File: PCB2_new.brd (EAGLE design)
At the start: 100 x 80 mm, 106 parts

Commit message: PCB2 for remote work
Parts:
- added R1, R2, R3: 330k, rcl:M0805
- moved H2 114.1 mm to (69.6, 19.6)
- moved H1 50.9 mm to (14.0, 11.4)
- moved SJ1 1.27 mm to (6.10, 19.9), flipped to the bottom, turned to 180 degrees
- moved SJ2 0.51 mm to (92.7, 18.5), flipped to the bottom, turned to 180 degrees
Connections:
- new net N$31: PAD3.1, R3.1
- net FRET3: now also R1.1, R1.2
- net FRET4: now also R2.1, R2.2
- net FRET5: now also R3.2; no longer PAD3.1
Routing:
- net VDD: track 0.00 -> 108.6 mm, vias 0 -> 2
- net FRET5: track 25.3 -> 14.7 mm, vias 0 -> 1
- net N$31: track 0.00 -> 9.09 mm
- net G: track 92.8 -> 98.6 mm
- net FRET4: track 65.4 -> 61.7 mm
- net GND: track 244.4 -> 246.4 mm
- net FRET3: track 89.9 -> 91.6 mm
- net LED_SER5: track 98.9 -> 97.6 mm
- net LED_SER6: track 52.2 -> 51.4 mm
- net RCK: track 67.9 -> 68.6 mm

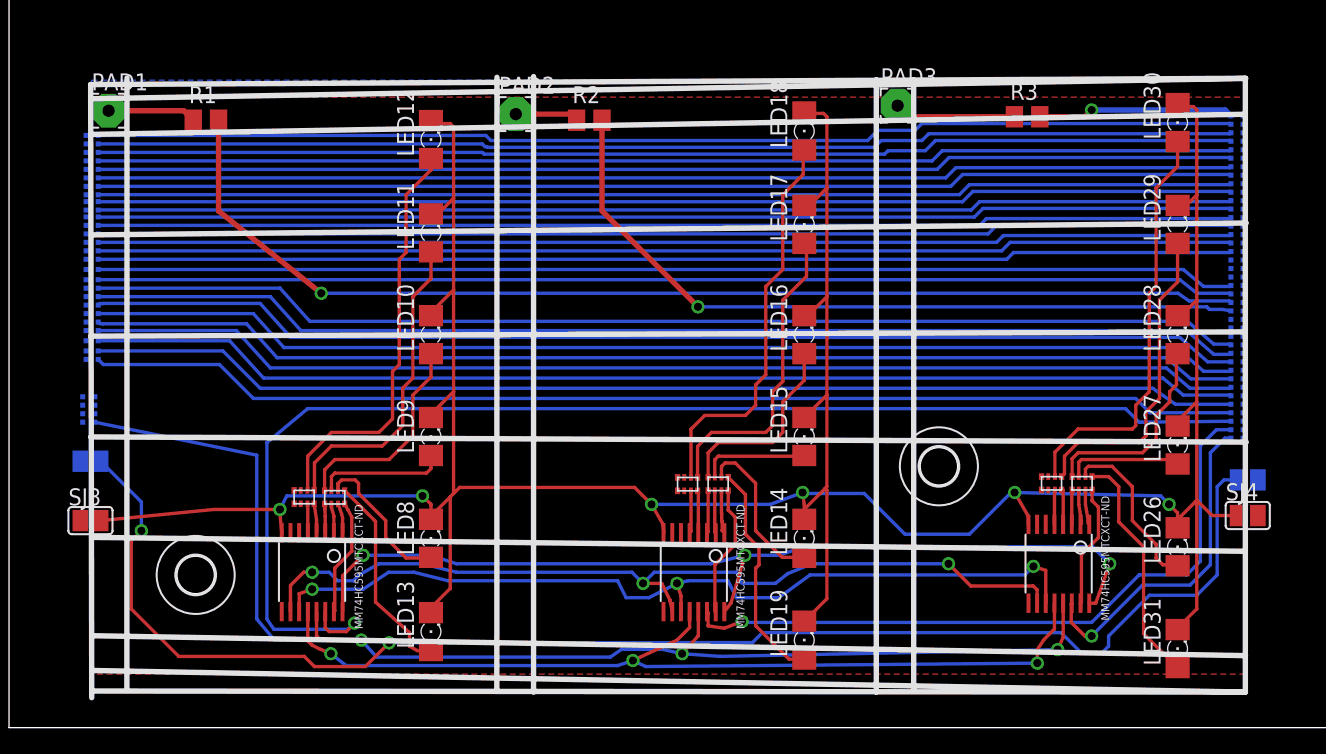
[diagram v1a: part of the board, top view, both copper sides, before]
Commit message: Finished changing dimensions for PCB3 and switched out resistors for smaller ones.
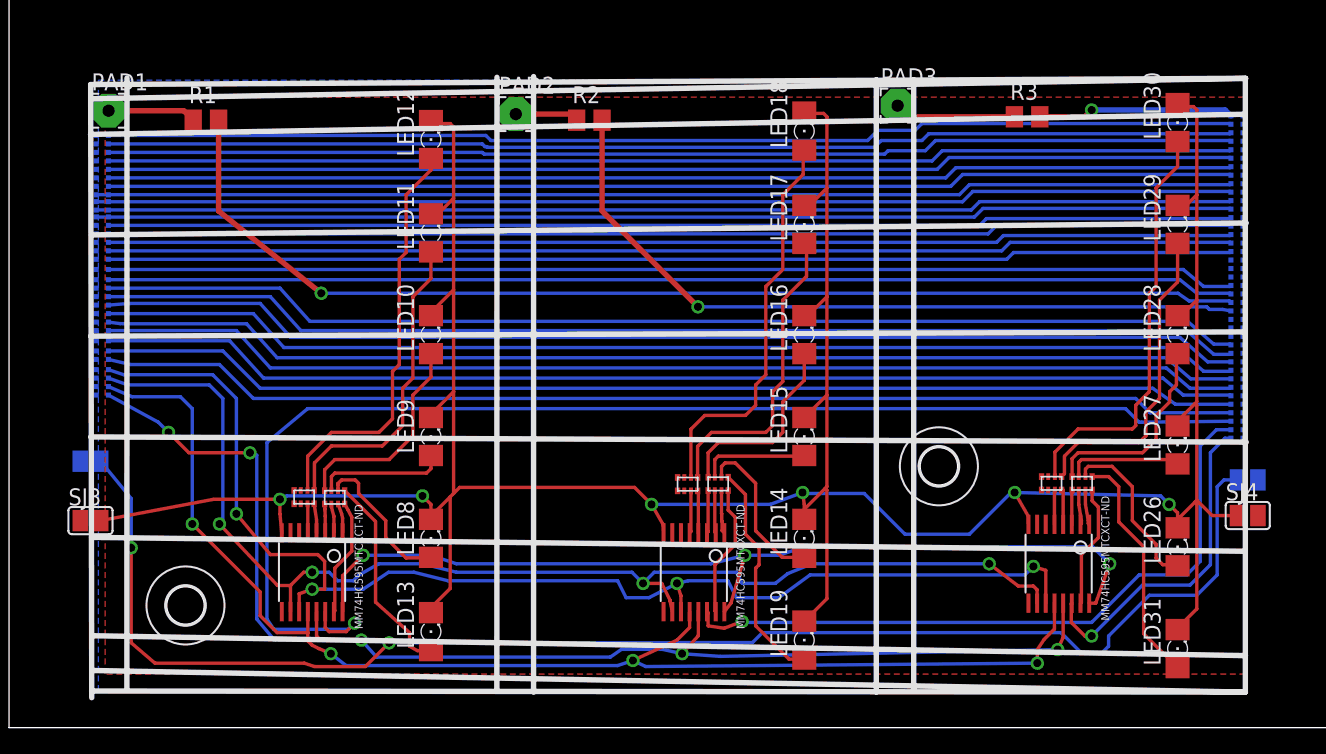
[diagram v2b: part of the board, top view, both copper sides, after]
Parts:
- moved H1 2.41 mm to (13.2, 9.14)
- moved U$70 2.27 mm to (6.99, 26.8)
- moved U$71 2.27 mm to (6.99, 26.2)
- moved U$72 2.27 mm to (6.99, 25.5)
- moved U$73 2.27 mm to (6.99, 24.9)
- moved U$43 0.76 mm to (6.98, 33.5)
- moved U$44 0.76 mm to (6.99, 38.7)
- moved U$45 0.76 mm to (6.99, 39.4)
- moved U$46 0.76 mm to (6.99, 38.2)
- moved U$47 0.76 mm to (6.99, 37.6)
- moved U$48 0.76 mm to (6.99, 27.6)
- moved U$49 0.76 mm to (6.99, 28.2)
- moved U$50 0.76 mm to (6.99, 32.9)
- moved U$51 0.76 mm to (6.99, 32.3)
- moved U$52 0.76 mm to (6.99, 31.6)
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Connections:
- removed net N$14: U$71.P$1, U$71.P$2
- removed net N$48: U$70.P$1, U$70.P$2
- removed net N$51: U$72.P$1, U$72.P$2
- net RCK: now also U$72.P$1, U$72.P$2
- net SCK: now also U$70.P$1, U$70.P$2
- net SCLR: now also U$71.P$1, U$71.P$2
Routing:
- net SCK: track 65.1 -> 95.3 mm, vias 3 -> 4
- net RCK: track 68.6 -> 97.1 mm, vias 3 -> 4
- net SCLR: track 66.1 -> 91.8 mm, vias 3 -> 4
- net P1_2: track 86.4 -> 85.6 mm
- net P2_4: track 86.5 -> 85.7 mm
- net TXD: track 85.3 -> 84.6 mm
- net RXD: track 85.5 -> 84.7 mm
- net RST_N: track 86.5 -> 85.7 mm
- net P3_6: track 85.2 -> 84.4 mm
- net P3_4: track 85.1 -> 84.4 mm
- net P3_3: track 85.2 -> 84.4 mm
- net P3_2: track 85.1 -> 84.4 mm
- net P3_1: track 85.3 -> 84.5 mm
- net P2_0: track 86.6 -> 85.8 mm
- net P1_7: track 86.5 -> 85.8 mm
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
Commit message: Modifying dimensions on PCB#_new boards
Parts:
- moved SJ1 0.25 mm to (6.10, 20.2), flipped to the top, turned to 0 degrees
- flipped SJ2 to the top
- flipped SJ3 to the bottom, turned to 180 degrees
- flipped SJ4 to the bottom
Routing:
- net GND: track 246.7 -> 255.9 mm, vias 6 -> 8
- net VDD: track 109.2 -> 106.5 mm, vias 2 -> 0

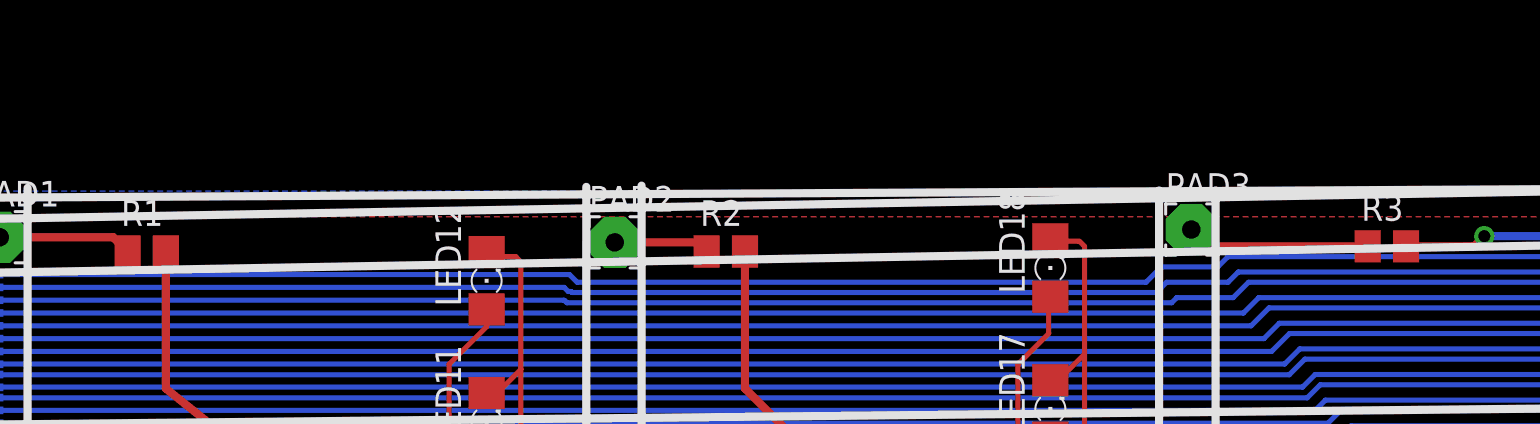
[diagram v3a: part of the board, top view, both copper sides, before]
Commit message: Updated ref des to match those in BOM
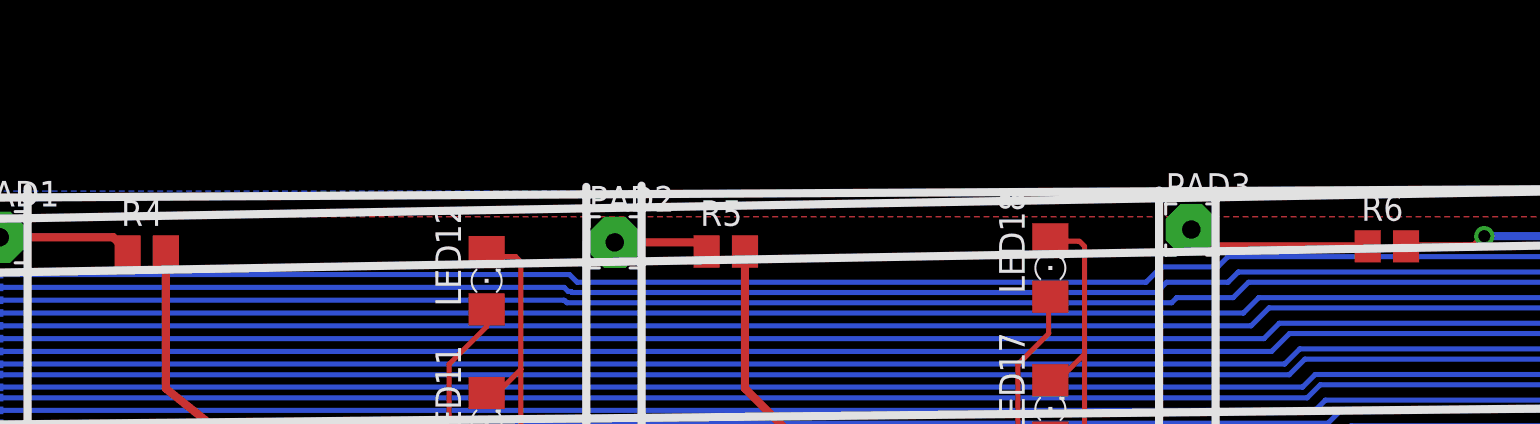
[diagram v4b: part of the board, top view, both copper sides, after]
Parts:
- renumbered R1 to R4, R2 to R5, R3 to R6
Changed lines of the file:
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@@
 <element name="U$78" library="ECE477_Guitutar" package="MNR04" value="MNR04MRAPJ680" x="80.264" y="18.288" rot="R180"/>
 <element name="U$79" library="ECE477_Guitutar" package="MNR04" value="MNR04MRAPJ680" x="77.978" y="18.288" rot="R180"/>
-<element name="R1" library="rcl" package="M0805" value="330k" x="14.732" y="45.466"/>
-<element name="R2" library="rcl" package="M0805" value="330k" x="43.434" y="45.466"/>
-<element name="R3" library="rcl" package="M0805" value="330k" x="76.2" y="45.72"/>
+<element name="R4" library="rcl" package="M0805" value="330k" x="14.732" y="45.466"/>
+<element name="R5" library="rcl" package="M0805" value="330k" x="43.434" y="45.466"/>
+<element name="R6" library="rcl" package="M0805" value="330k" x="76.2" y="45.72"/>
 </elements>
 <signals>
@@
 <wire x1="87.49141875" y1="32.512" x2="23.368" y2="32.512" width="0.254" layer="16"/>
 <via x="23.368" y="32.512" extent="1-16" drill="0.6"/>
-<contactref element="R1" pad="1"/>
-<contactref element="R1" pad="2"/>
+<contactref element="R4" pad="1"/>
+<contactref element="R4" pad="2"/>
 <wire x1="7.45" y1="46.174" x2="13.074" y2="46.174" width="0.4064" layer="1"/>
 <wire x1="13.074" y1="46.174" x2="13.782" y2="45.466" width="0.4064" layer="1"/>
@@
 <wire x1="89.8325375" y1="31.3023" x2="89.6388375" y2="31.496" width="0.254" layer="16"/>
 <via x="51.562" y="31.496" extent="1-16" drill="0.6"/>
-<contactref element="R2" pad="1"/>
+<contactref element="R5" pad="1"/>
 <wire x1="37.93" y1="45.92" x2="42.03" y2="45.92" width="0.4064" layer="1"/>
 <wire x1="42.03" y1="45.92" x2="42.484" y2="45.466" width="0.4064" layer="1"/>
-<contactref element="R2" pad="2"/>
+<contactref element="R5" pad="2"/>
 <wire x1="44.384" y1="45.466" x2="44.384" y2="38.674" width="0.4064" layer="1"/>
 <wire x1="44.384" y1="38.674" x2="51.562" y2="31.496" width="0.4064" layer="1"/>
@@
 <signal name="FRET5">
 <contactref element="U$2" pad="P$2"/>
-<contactref element="R3" pad="2"/>
+<contactref element="R6" pad="2"/>
 <wire x1="77.15" y1="45.72" x2="80.518" y2="45.72" width="0.4064" layer="1"/>
 <wire x1="80.518" y1="45.72" x2="81.026" y2="46.228" width="0.4064" layer="1"/>
@@
 <signal name="N$31">
 <contactref element="PAD3" pad="1"/>
-<contactref element="R3" pad="1"/>
+<contactref element="R6" pad="1"/>
 <wire x1="75.25" y1="45.72" x2="67.34" y2="45.72" width="0.4064" layer="1"/>
 <wire x1="67.34" y1="45.72" x2="66.505" y2="46.555" width="0.4064" layer="1"/>

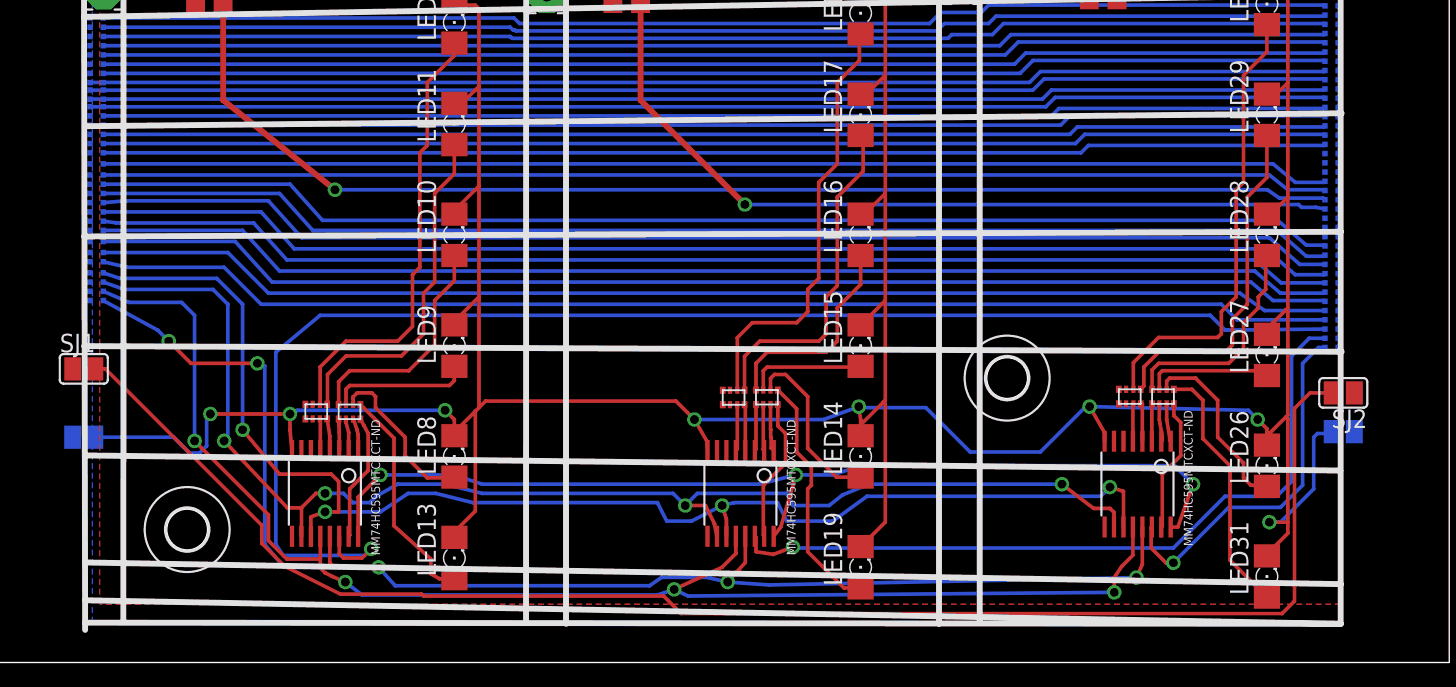
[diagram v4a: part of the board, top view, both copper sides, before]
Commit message: Fixed pin distances for PCB2 and added shift register pins to the right side of board
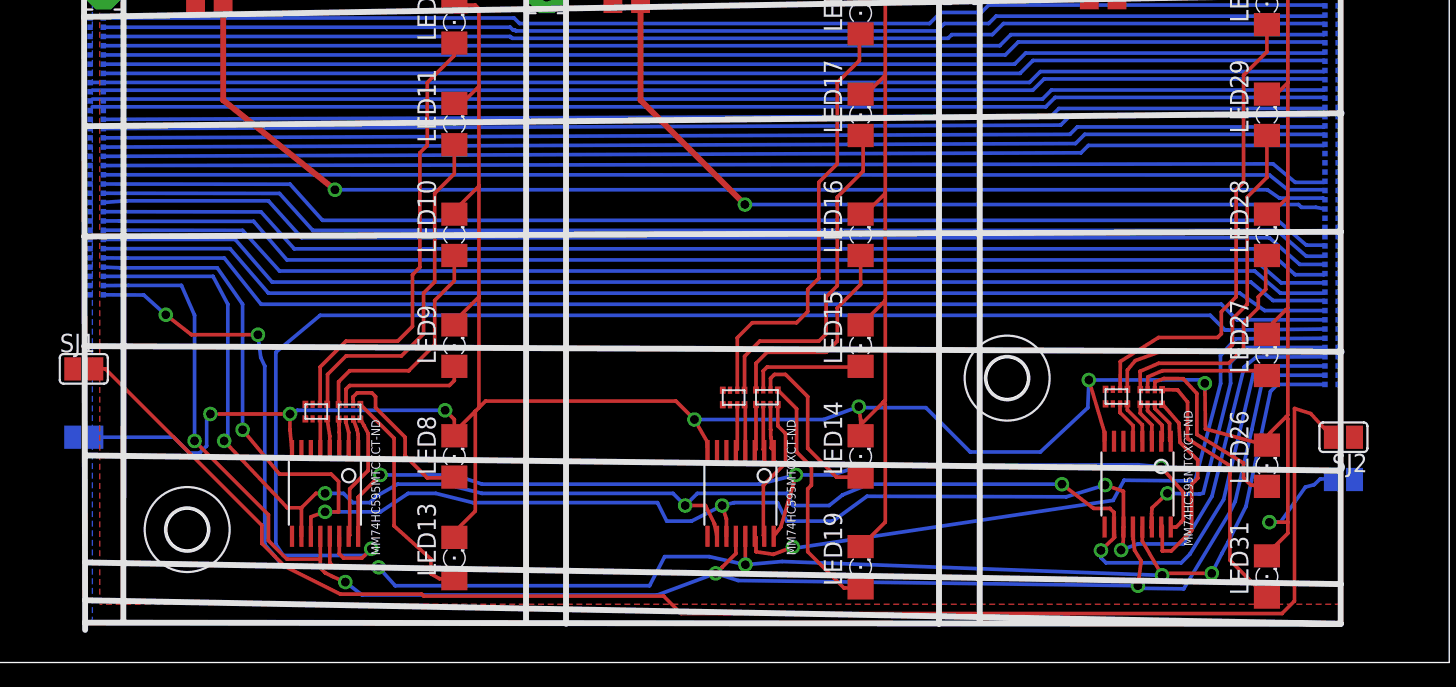
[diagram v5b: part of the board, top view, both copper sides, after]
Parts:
- added U$80, U$81, U$82, U$83: JUMPER, ECE477_Guitutar:JUMPER
- moved SJ4 3.29 mm to (92.7, 12.6)
- moved SJ2 3.05 mm to (92.7, 15.5)
- moved U$79 0.91 mm to (77.1, 18.3)
- moved U$78 0.81 mm to (79.5, 18.3)
- moved U$71 0.39 mm to (6.99, 26.6)
- moved U$70 0.39 mm to (6.99, 27.2)
- moved U$72 0.39 mm to (6.99, 25.9)
- moved U$73 0.39 mm to (6.99, 25.3)
- moved U$46 0.27 mm to (6.99, 38.0)
- moved U$48 0.27 mm to (6.99, 27.8)
- moved U$49 0.27 mm to (6.99, 28.5)
- moved U$66 0.24 mm to (6.99, 36.7)
- moved U$67 0.24 mm to (6.99, 36.1)
- moved U$69 0.24 mm to (6.99, 34.8)
- moved U$47 0.24 mm to (6.99, 37.4)
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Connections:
- net G: now also U$83.P$1, U$83.P$2
- net RCK: now also U$82.P$1, U$82.P$2
- net SCK: now also U$80.P$1, U$80.P$2
- net SCLR: now also U$81.P$1, U$81.P$2
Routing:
- net SCLR: track 91.8 -> 119.9 mm, vias 4 -> 5
- net SCK: track 95.3 -> 120.5 mm, vias 4 -> 5
- net G: track 98.9 -> 122.0 mm, vias 5 -> 6
- net RCK: track 97.1 -> 119.1 mm
- net N$66: track 9.80 -> 14.8 mm
- net LED_SER7: track 24.9 -> 21.5 mm
- net GND: track 255.9 -> 258.8 mm
- net LED_SER6: track 51.4 -> 49.0 mm
- net VCC: track 69.7 -> 68.7 mm
- net N$71: track 23.7 -> 24.5 mm
- net N$17: track 31.3 -> 32.0 mm
- net N$18: track 15.3 -> 16.0 mm
- net N$68: track 12.7 -> 13.4 mm
- net N$69: track 8.69 -> 9.30 mm
- net N$67: track 17.7 -> 18.2 mm

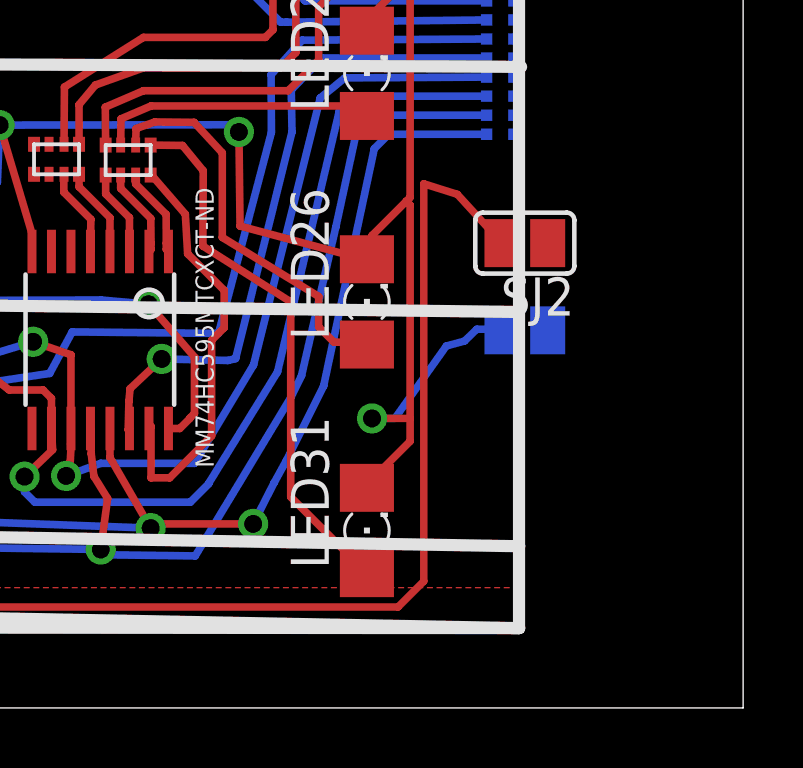
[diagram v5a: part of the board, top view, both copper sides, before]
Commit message: Finished PCB3 checks and added traces for shift registers
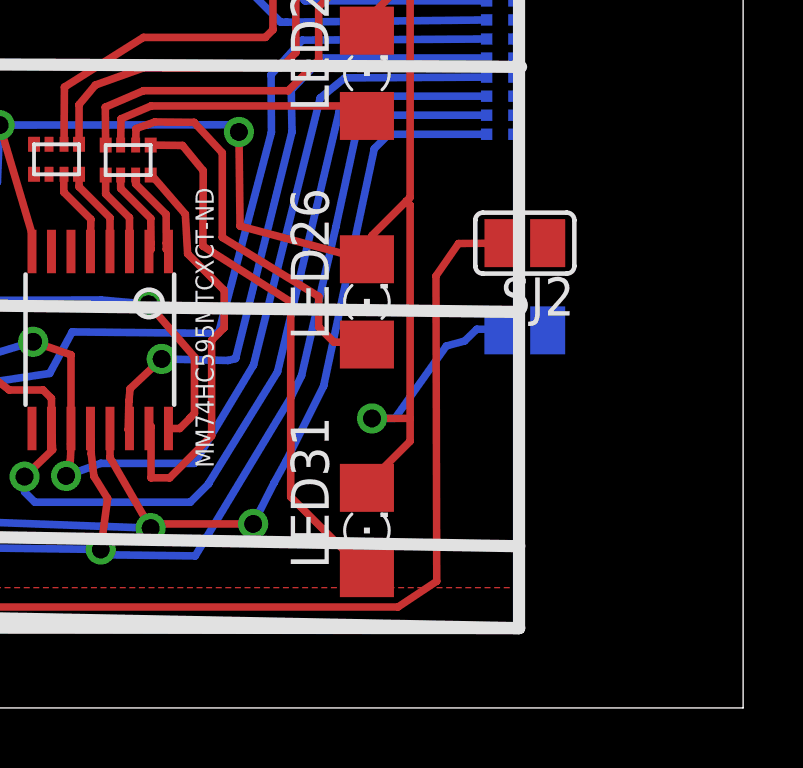
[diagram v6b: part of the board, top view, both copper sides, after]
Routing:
- net VDD: track 106.8 -> 103.5 mm
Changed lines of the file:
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@@
 <wire x1="45.97121875" y1="4.572" x2="47.17841875" y2="3.3648" width="0.25" layer="1"/>
 <wire x1="47.17841875" y1="3.3648" x2="88.49744375" y2="3.3648" width="0.25" layer="1"/>
-<wire x1="88.49744375" y1="3.3648" x2="89.3552" y2="4.22255625" width="0.25" layer="1"/>
-<wire x1="89.3552" y1="17.4732" x2="90.4748" y2="17.1196" width="0.25" layer="1"/>
-<wire x1="90.4748" y1="17.1196" x2="91.9607" y2="15.494" width="0.25" layer="1"/>
-<wire x1="89.3552" y1="4.22255625" x2="89.3552" y2="17.4732" width="0.25" layer="1"/>
+<wire x1="88.49744375" y1="3.3648" x2="89.787" y2="4.22255625" width="0.25" layer="1"/>
+<wire x1="89.7616" y1="14.3998" x2="90.5129" y2="15.4813" width="0.25" layer="1"/>
+<wire x1="90.5129" y1="15.4813" x2="91.9607" y2="15.494" width="0.25" layer="1"/>
+<wire x1="89.787" y1="4.22255625" x2="89.7616" y2="14.3998" width="0.25" layer="1"/>
 <wire x1="91.9607" y1="15.494" x2="93.4847" y2="15.494" width="0" layer="19" extent="1-1"/>
 <wire x1="5.334" y1="20.193" x2="6.858" y2="20.193" width="0" layer="19" extent="1-1"/>

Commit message: Finished PCB4. Finished gerbers for PCB1, 2, 3, and 4
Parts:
- moved H1 1.17 mm to (12.1, 8.66)
- moved LED31 1.02 mm to (87.5, 6.93)
- moved LED19 0.88 mm to (59.5, 7.43)
- moved LED13 0.23 mm to (31.5, 7.41)
- moved U$78 0.23 mm to (79.7, 18.3)
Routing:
- net RCK: track 119.1 -> 123.1 mm
- net VDD: track 103.5 -> 102.3 mm
- net N$67: track 18.2 -> 17.4 mm
- net G: track 122.0 -> 121.3 mm
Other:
- board size 100 x 80 mm -> 100.1 x 51 mm
